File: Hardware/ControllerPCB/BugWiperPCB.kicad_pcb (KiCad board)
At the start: 4 copper layers, 110 x 40 mm, 107 parts, among them J1 UJ20-C-H-G-SMT-1-P16-TR, J2 1770924, J3 Phoenix_1776508, J4 RJ45, J5 Conn_TagConnect_TC2030-NL_ESP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, J6 1824420000, J7 Conn_01x02_Pin, Q1 NMOS_SO-8, U1 ESP32-S3-WROOM-1, U2 BTN9960LV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

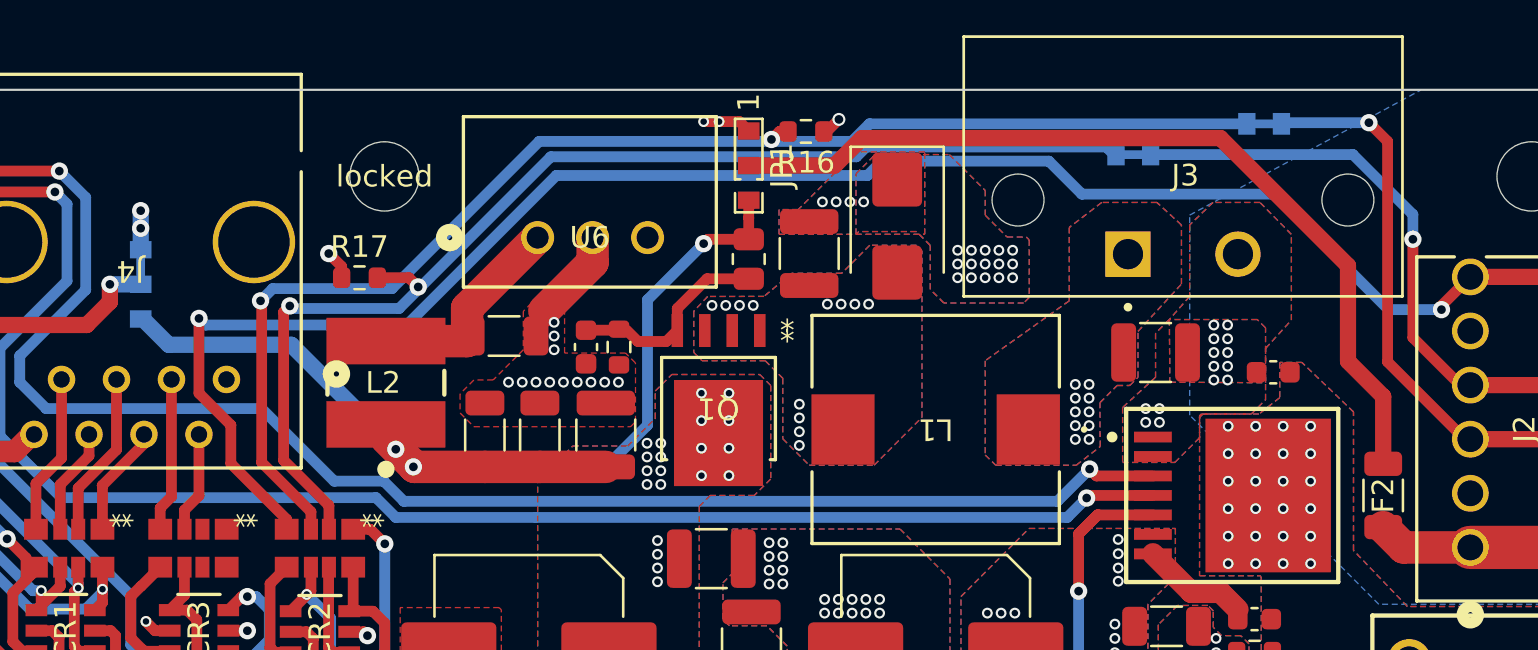
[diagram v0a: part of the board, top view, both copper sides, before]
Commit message: update PCB and add a second PCB as a Controlpanel with a dual toggle switch and rgb LED
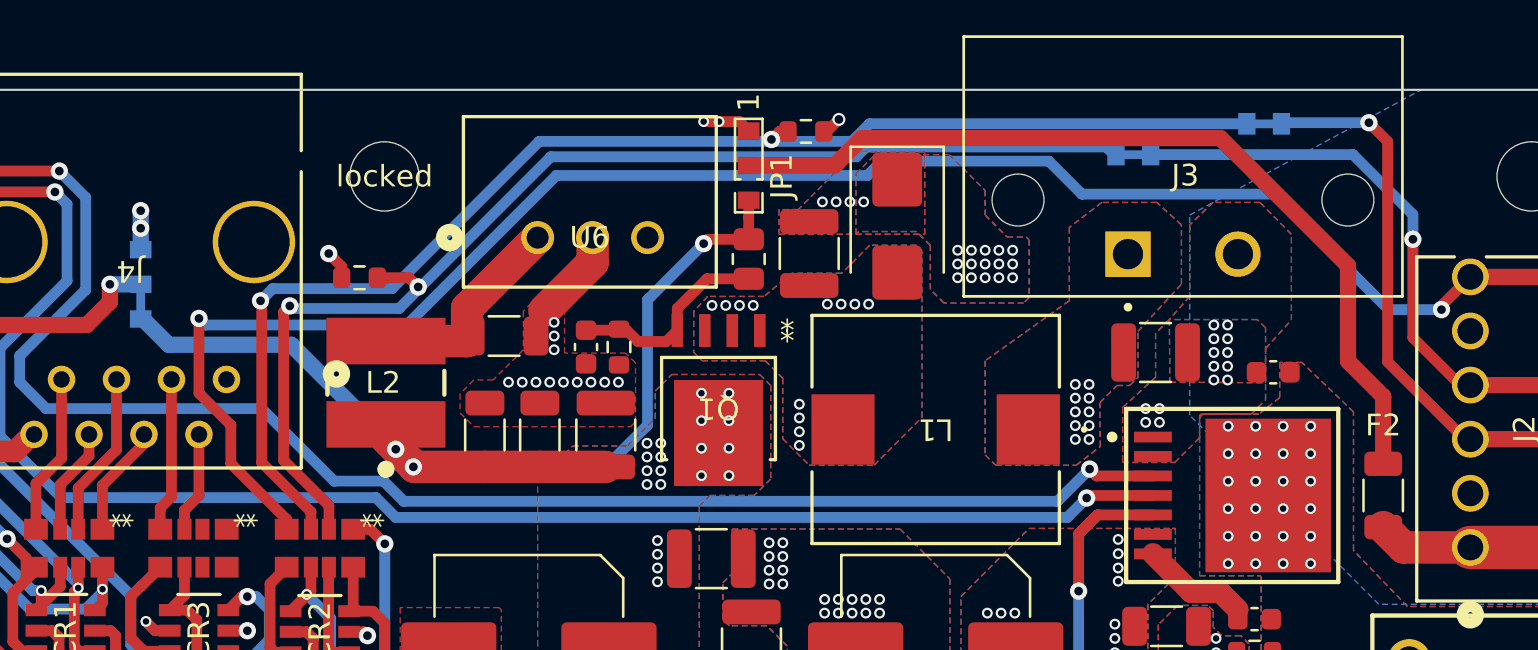
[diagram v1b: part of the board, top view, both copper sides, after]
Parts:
- turned JP4 to 90 degrees
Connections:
- JP4 pad 1: +3.3V -> +12V
- JP4 pad 3: +12V -> +3.3V
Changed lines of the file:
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@@
       (net 53 "Net-(CR1-IO_1)") (pinfunction "IO_1") (pintype "unspecified"))
     (pad "2" smd rect (at -1.35255 0) (size 1.0033 0.5588) (layers "F.Cu" "F.Paste" "F.Mask")
-      (net 17 "GND") (pinfunction "Vss") (pintype "unspecified"))
+      (net 17 "GND") (pinfunction "Vss") (pintype "power_in"))
     (pad "3" smd rect (at -1.35255 0.950001) (size 1.0033 0.5588) (layers "F.Cu" "F.Paste" "F.Mask")
       (net 36 "Net-(CR1-IO_2)") (pinfunction "IO_2") (pintype "unspecified"))
@@
       (net 41 "Net-(CR1-IO_3)") (pinfunction "IO_3") (pintype "unspecified"))
     (pad "5" smd rect (at 1.35255 0) (size 1.0033 0.5588) (layers "F.Cu" "F.Paste" "F.Mask")
-      (net 47 "+3.3V") (pinfunction "Vcc") (pintype "unspecified"))
+      (net 47 "+3.3V") (pinfunction "Vcc") (pintype "power_in"))
     (pad "6" smd rect (at 1.35255 -0.950001) (size 1.0033 0.5588) (layers "F.Cu" "F.Paste" "F.Mask")
       (net 42 "Net-(CR1-IO_4)") (pinfunction "IO_4") (pintype "unspecified"))
@@
       (net 11 "unconnected-(U1-SPIDQS{slash}GPIO37{slash}FSPIQ{slash}SUBSPIQ-Pad30)") (pinfunction "SPIDQS/GPIO37/FSPIQ/SUBSPIQ") (pintype "bidirectional+no_connect"))
     (pad "31" smd rect locked (at 8.75 3.17) (size 1.5 0.9) (layers "F.Cu" "F.Paste" "F.Mask")
-      (net 12 "unconnected-(U1-GPIO38{slash}FSPIWP{slash}SUBSPIWP-Pad31)") (pinfunction "GPIO38/FSPIWP/SUBSPIWP") (pintype "bidirectional"))
+      (net 12 "unconnected-(U1-GPIO38{slash}FSPIWP{slash}SUBSPIWP-Pad31)") (pinfunction "GPIO38/FSPIWP/SUBSPIWP") (pintype "bidirectional+no_connect"))
     (pad "32" smd rect locked (at 8.75 1.9) (size 1.5 0.9) (layers "F.Cu" "F.Paste" "F.Mask")
       (net 13 "unconnected-(U1-MTCK{slash}GPIO39{slash}CLK_OUT3{slash}SUBSPICS1-Pad32)") (pinfunction "MTCK/GPIO39/CLK_OUT3/SUBSPICS1") (pintype "bidirectional+no_connect"))
@@
       (net 3 "TX") (pinfunction "U0TXD/GPIO43/CLK_OUT1") (pintype "bidirectional"))
     (pad "38" smd rect locked (at 8.75 -5.72) (size 1.5 0.9) (layers "F.Cu" "F.Paste" "F.Mask")
-      (net 76 "unconnected-(U1-GPIO2{slash}TOUCH2{slash}ADC1_CH1-Pad38)") (pinfunction "GPIO2/TOUCH2/ADC1_CH1") (pintype "bidirectional"))
+      (net 76 "unconnected-(U1-GPIO2{slash}TOUCH2{slash}ADC1_CH1-Pad38)") (pinfunction "GPIO2/TOUCH2/ADC1_CH1") (pintype "bidirectional+no_connect"))
     (pad "39" smd rect locked (at 8.75 -6.99) (size 1.5 0.9) (layers "F.Cu" "F.Paste" "F.Mask")
       (net 74 "A_INA") (pinfunction "GPIO1/TOUCH1/ADC1_CH0") (pintype "bidirectional"))
@@
       (net 91 "OUT_1") (pinfunction "IO_1") (pintype "unspecified"))
     (pad "2" smd rect (at -1.35255 0) (size 1.0033 0.5588) (layers "F.Cu" "F.Paste" "F.Mask")
-      (net 17 "GND") (pinfunction "Vss") (pintype "unspecified"))
+      (net 17 "GND") (pinfunction "Vss") (pintype "power_in"))
     (pad "3" smd rect (at -1.35255 0.950001) (size 1.0033 0.5588) (layers "F.Cu" "F.Paste" "F.Mask")
       (net 92 "OUT_2") (pinfunction "IO_2") (pintype "unspecified"))
@@
       (net 61 "/ESP32-S3/M_IS2") (pinfunction "IO_3") (pintype "unspecified"))
     (pad "5" smd rect (at 1.35255 0) (size 1.0033 0.5588) (layers "F.Cu" "F.Paste" "F.Mask")
-      (net 47 "+3.3V") (pinfunction "Vcc") (pintype "unspecified"))
+      (net 47 "+3.3V") (pinfunction "Vcc") (pintype "power_in"))
     (pad "6" smd rect (at 1.35255 -0.950001) (size 1.0033 0.5588) (layers "F.Cu" "F.Paste" "F.Mask")
       (net 60 "/ESP32-S3/M_IS1") (pinfunction "IO_4") (pintype "unspecified"))
@@
       (net 78 "Net-(CR2-IO_1)") (pinfunction "IO_1") (pintype "unspecified"))
     (pad "2" smd rect (at -1.35255 0) (size 1.0033 0.5588) (layers "F.Cu" "F.Paste" "F.Mask")
-      (net 17 "GND") (pinfunction "Vss") (pintype "unspecified"))
+      (net 17 "GND") (pinfunction "Vss") (pintype "power_in"))
     (pad "3" smd rect (at -1.35255 0.950001) (size 1.0033 0.5588) (layers "F.Cu" "F.Paste" "F.Mask")
       (net 50 "Net-(CR2-IO_2)") (pinfunction "IO_2") (pintype "unspecified"))
@@
       (net 44 "Net-(CR2-IO_3)") (pinfunction "IO_3") (pintype "unspecified"))
     (pad "5" smd rect (at 1.35255 0) (size 1.0033 0.5588) (layers "F.Cu" "F.Paste" "F.Mask")
-      (net 47 "+3.3V") (pinfunction "Vcc") (pintype "unspecified"))
+      (net 47 "+3.3V") (pinfunction "Vcc") (pintype "power_in"))
     (pad "6" smd rect (at 1.35255 -0.950001) (size 1.0033 0.5588) (layers "F.Cu" "F.Paste" "F.Mask")
       (net 77 "Net-(CR2-IO_4)") (pinfunction "IO_4") (pintype "unspecified"))
@@
       (stroke (width 0.0254) (type solid)) (layer "F.Fab"))
     (pad "1" smd rect (at -0.8763 -1.5367 270) (size 0.9652 1.1) (layers "F.Cu" "F.Paste" "F.Mask")
-      (net 89 "unconnected-(RN3A-R1.1-Pad1)") (pinfunction "R1.1") (pintype "passive"))
+      (net 89 "unconnected-(RN3A-R1.1-Pad1)") (pinfunction "R1.1") (pintype "passive+no_connect"))
     (pad "2" smd rect (at -0.8763 -0.41529 270) (size 0.9652 0.65) (layers "F.Cu" "F.Paste" "F.Mask")
-      (net 90 "unconnected-(RN3B-R2.1-Pad2)") (pinfunction "R2.1") (pintype "passive"))
+      (net 90 "unconnected-(RN3B-R2.1-Pad2)") (pinfunction "R2.1") (pintype "passive+no_connect"))
     (pad "3" smd rect (at -0.8763 0.41402 270) (size 0.9652 0.65) (layers "F.Cu" "F.Paste" "F.Mask")
       (net 96 "Net-(RN3C-R3.1)") (pinfunction "R3.1") (pintype "passive"))
@@
       (net 91 "OUT_1") (pinfunction "R3.2") (pintype "passive"))
     (pad "7" smd rect (at 0.8763 -0.41402 270) (size 0.9652 0.65) (layers "F.Cu" "F.Paste" "F.Mask")
-      (net 93 "unconnected-(RN3B-R2.2-Pad7)") (pinfunction "R2.2") (pintype "passive"))
+      (net 93 "unconnected-(RN3B-R2.2-Pad7)") (pinfunction "R2.2") (pintype "passive+no_connect"))
     (pad "8" smd rect (at 0.8763 -1.5367 270) (size 0.9652 1.1) (layers "F.Cu" "F.Paste" "F.Mask")
-      (net 94 "unconnected-(RN3A-R1.2-Pad8)") (pinfunction "R1.2") (pintype "passive"))
+      (net 94 "unconnected-(RN3A-R1.2-Pad8)") (pinfunction "R1.2") (pintype "passive+no_connect"))
     (model "${KIPRJMOD}/lib/BO_CAY16.step"
       (offset (xyz 0 0 0))
@@
     (property "ki_keywords" "R res resistor")
     (attr smd)
-    (fp_text reference "R16" (at 0 -1.43) (layer "F.SilkS")
+    (fp_text reference "R16" (at 0 -1.43) (layer "F.SilkS") hide
         (effects (font (size 1 1) (thickness 0.15)))
     )
@@
       (net 29 "Net-(J1-DN1)") (pinfunction "DN1") (pintype "passive"))
     (pad "A8" smd rect locked (at 1.25 -7.345 180) (size 0.3 1.15) (layers "F.Cu" "F.Paste" "F.Mask")
-      (net 24 "unconnected-(J1-SBU1-PadA8)") (pinfunction "SBU1") (pintype "passive"))
+      (net 24 "unconnected-(J1-SBU1-PadA8)") (pinfunction "SBU1") (pintype "passive+no_connect"))
     (pad "B1_A12" smd rect locked (at 3.2 -7.36 180) (size 0.6 1.1) (layers "F.Cu" "F.Paste" "F.Mask")
       (net 17 "GND") (pinfunction "GND") (pintype "passive"))
@@
       (net 29 "Net-(J1-DN1)") (pinfunction "DN2") (pintype "passive"))
     (pad "B8" smd rect locked (at -1.75 -7.345 180) (size 0.3 1.15) (layers "F.Cu" "F.Paste" "F.Mask")
-      (net 25 "unconnected-(J1-SBU2-PadB8)") (pinfunction "SBU2") (pintype "passive"))
+      (net 25 "unconnected-(J1-SBU2-PadB8)") (pinfunction "SBU2") (pintype "passive+no_connect"))
     (pad "SH1" thru_hole oval locked (at -4.32 -6.78 180) (size 1 2.1) (drill oval 0.6 1.7) (layers "*.Cu" "*.Mask")
       (net 28 "Net-(J1-SHIELD-PadSH1)") (pinfunction "SHIELD") (pintype "passive") (solder_mask_margin 0.102))
@@
     (property "ki_keywords" "resettable fuse PTC PPTC polyfuse polyswitch")
     (attr smd)
-    (fp_text reference "F2" (at 0 0 90) (layer "F.SilkS")
+    (fp_text reference "F2" (at 3.24 0 180) (layer "F.SilkS")
         (effects (font (size 1 1) (thickness 0.15)))
     )
@@
     (property "ki_keywords" "Solder Jumper SPDT")
     (attr exclude_from_pos_files)
-    (fp_text reference "JP1" (at 0 -1.524 90) (layer "F.SilkS")
+    (fp_text reference "JP1" (at 0.5 -1.524 90) (layer "F.SilkS")
         (effects (font (size 1 1) (thickness 0.15)))
     )
@@
     (property "ki_keywords" "R res resistor")
     (attr smd)
-    (fp_text reference "R17" (at 0 -1.43) (layer "F.SilkS")
+    (fp_text reference "R17" (at 0 -1.43) (layer "F.SilkS") hide
         (effects (font (size 1 1) (thickness 0.15)))
     )
@@
   )
   (footprint "BugWiper_lib:SolderJumper_3P_R_SMD_0603_Bridged_12" (layer "B.Cu")
-    (at 151.7396 68.9864 -90)
+    (at 151.7396 68.9864 90)
     (descr "SMD Solder Jumper, 1x1.5mm Pads, 0.3mm gap, open, labeled with numbers")
     (tags "solder jumper open")
@@
     (fp_line (start 2.286 -0.762) (end 2.286 0.762)
       (stroke (width 0.05) (type solid)) (layer "B.CrtYd"))
-    (pad "1" smd rect (at -1.6 0 270) (size 0.8 1) (layers "B.Cu" "B.Mask")
-      (net 47 "+3.3V") (pinfunction "A") (pintype "passive"))
-    (pad "2" smd rect (at 0 0 270) (size 0.8 1) (layers "B.Cu" "B.Mask")
+    (pad "1" smd rect (at -1.6 0 90) (size 0.8 1) (layers "B.Cu" "B.Mask")
+      (net 31 "+12V") (pinfunction "A") (pintype "passive"))
+    (pad "2" smd rect (at 0 0 90) (size 0.8 1) (layers "B.Cu" "B.Mask")
       (net 97 "Net-(JP4-C)") (pinfunction "C") (pintype "passive"))
-    (pad "3" smd rect (at 1.6 0 270) (size 0.8 1) (layers "B.Cu" "B.Mask")
-      (net 31 "+12V") (pinfunction "B") (pintype "passive"))
+    (pad "3" smd rect (at 1.6 0 90) (size 0.8 1) (layers "B.Cu" "B.Mask")
+      (net 47 "+3.3V") (pinfunction "B") (pintype "passive"))
     (model "${KIPRJMOD}/lib/RC0603.step"
       (offset (xyz -0.8 0 0))

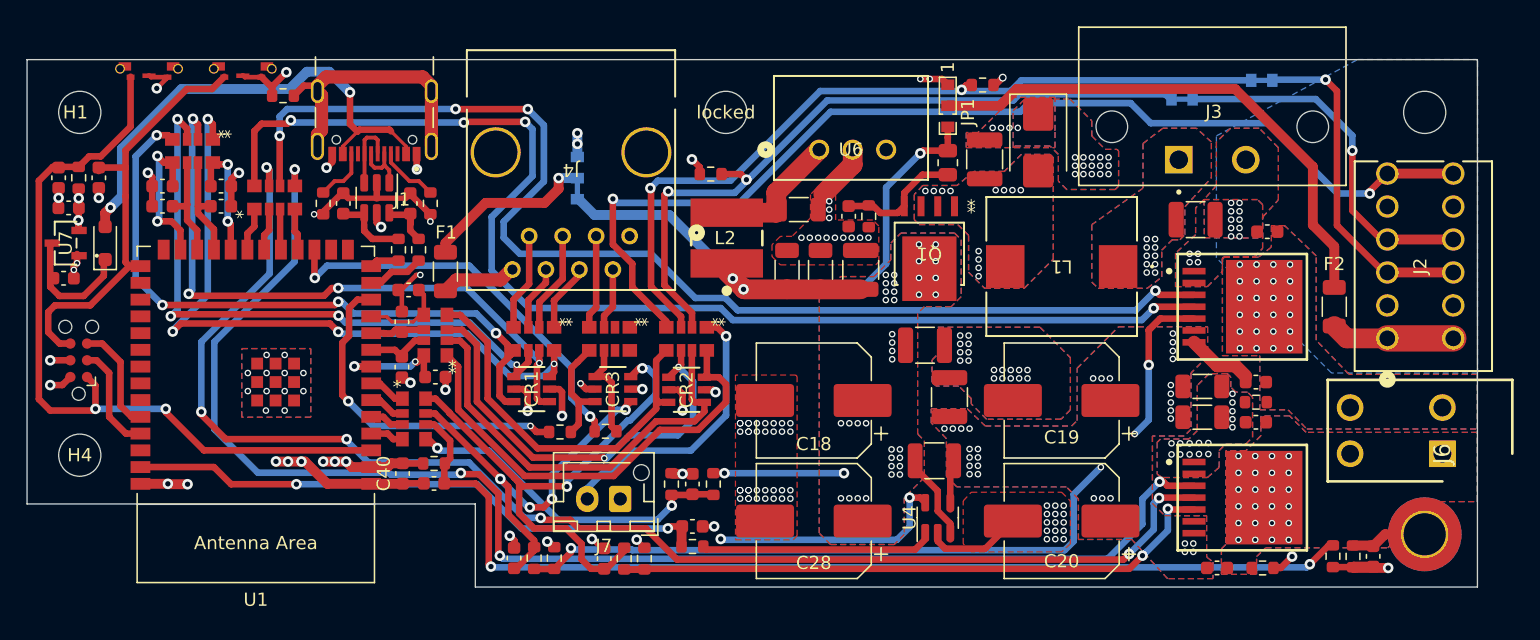
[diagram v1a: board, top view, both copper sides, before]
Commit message: Add a micro SD Card slot to the bottom of the controller board
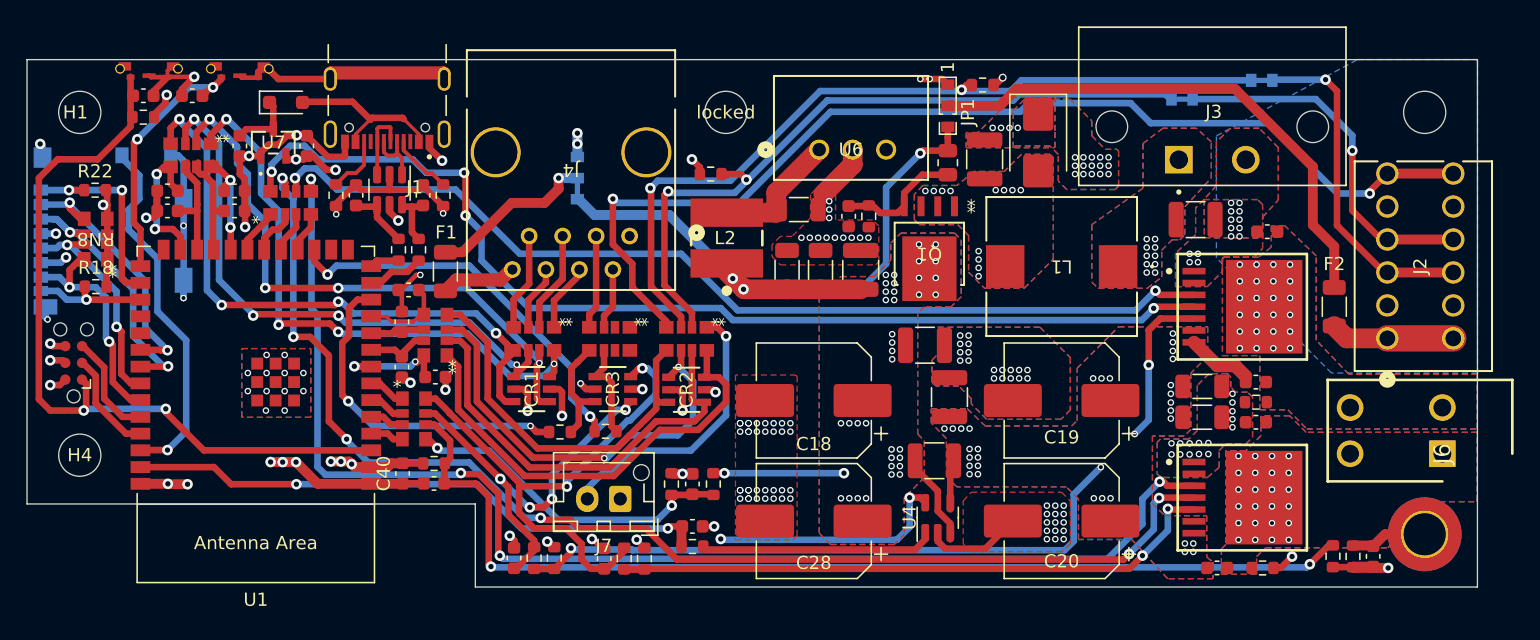
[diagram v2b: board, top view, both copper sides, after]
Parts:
- removed R1: 150k, Resistor_SMD:R_0603_1608Metric
- added J8: Micro_SD_Card, BugWiper_lib:microSD_HC_Molex_104031-0811, B.Cu at (116.5, 73.0)
- added R18: 10k, Resistor_SMD:R_0603_1608Metric, F.Cu at (115.2, 77.2)
- added R22: 10k, Resistor_SMD:R_0603_1608Metric, F.Cu at (115.2, 69.9)
- added RN8: 1k_Pack04, BugWiper_lib:BO_CAY16, F.Cu at (115.2, 73.6)
- moved C29 18.7 mm to (131.2, 66.5), turned to 90 degrees
- moved U7 17.5 mm to (128.7, 66.3), turned to 0 degrees
- moved D1 17.4 mm to (129.6, 63.2), turned to 0 degrees
- moved C30 16.7 mm to (126.1, 66.5), turned to -90 degrees
- moved C3 9.43 mm to (122.5, 62.7), turned to 180 degrees
- moved C4 8.95 mm to (118.8, 62.7), turned to 0 degrees
- moved R6 6.72 mm to (118.8, 64.4), turned to 0 degrees
- moved J1 1.34 mm to (137.3, 58.9)
- moved RN1 1.29 mm to (130.0, 70.9)
- moved U5 1.15 mm to (137.5, 69.9)
- moved C1 1.15 mm to (135.0, 70.3)
- moved C2 1.15 mm to (140.0, 70.3)
- moved R2 1.15 mm to (141.6, 70.3)
- moved R3 1.15 mm to (133.4, 70.3)
- moved C32 1.08 mm to (125.7, 70.0)
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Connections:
- net /ESP32-S3/M_IHN2 renamed /ESP32-S3/M_INH2
- J1 pad SH1: Net-(J1-SHIELD-PadSH1) -> GND
- J1 pad SH2: Net-(J1-SHIELD-PadSH1) -> GND
- J1 pad SH3: Net-(J1-SHIELD-PadSH1) -> GND
- J1 pad SH4: Net-(J1-SHIELD-PadSH1) -> GND
- U1 pad 28: unconnected-(U1-SPIIO6/GPIO35/FSPID/SUBSPID-Pad28) -> DAT2
- U1 pad 29: unconnected-(U1-SPIIO7/GPIO36/FSPICLK/SUBSPICLK-Pad29) -> DAT1
- U1 pad 32: unconnected-(U1-MTCK/GPIO39/CLK_OUT3/SUBSPICS1-Pad32) -> SD_CS
- U1 pad 33: unconnected-(U1-MTDO/GPIO40/CLK_OUT2-Pad33) -> MOSI
- U1 pad 34: unconnected-(U1-MTDI/GPIO41/CLK_OUT1-Pad34) -> CLK
- U1 pad 35: unconnected-(U1-MTMS/GPIO42-Pad35) -> MISO
- U1 pad 38: unconnected-(U1-GPIO2/TOUCH2/ADC1_CH1-Pad38) -> SD_DET
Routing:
- net GND: track 89.5 -> 133.8 mm, vias 173 -> 174
- net SD_DET: track 0.00 -> 27.7 mm, vias 0 -> 1
- net Net-(D1-A): track 36.7 -> 12.4 mm, vias 2 -> 0
- net MOSI: track 0.00 -> 20.9 mm, vias 0 -> 2
- net SD_CS: track 0.00 -> 20.1 mm, vias 0 -> 2
- net Net-(J1-SHIELD-PadSH1): track 19.9 -> 0.00 mm
- net MISO: track 0.00 -> 17.4 mm, vias 0 -> 2
- net /ESP32-S3/M_IN2: track 91.2 -> 74.7 mm, vias 4 -> 2
- net CLK: track 0.00 -> 16.4 mm, vias 0 -> 2
- net DAT2: track 0.00 -> 15.3 mm, vias 0 -> 2
- net /ESP32-S3/M_INH2: track 93.1 -> 81.6 mm
- net /ESP32-S3/M_INH1: track 105.6 -> 94.9 mm
- net +3.3V: track 41.8 -> 52.3 mm, vias 16 -> 19
- net /ESP32-S3/M_IN1: track 108.3 -> 98.8 mm
- net Boot: track 32.8 -> 42.2 mm, vias 0 -> 3
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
